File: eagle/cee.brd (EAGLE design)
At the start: 50 x 80 mm, 54 parts, among them IC1 IC1, J1 SOLDERJUMPERNC2

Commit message: Clean up around DAC
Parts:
- moved DAC 3.16 mm to (10.0, 32.0)
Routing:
- net 2.5VREF: track 82.8 -> 71.2 mm, vias 4 -> 3
- net LDAC: track 3.73 -> 6.99 mm
- net VOUT-B: track 22.4 -> 25.7 mm
- net VOUT-A: track 38.5 -> 41.2 mm
- net CS: track 14.9 -> 17.3 mm
- net SCK: track 15.2 -> 17.5 mm
- net MOSI: track 15.6 -> 17.6 mm
- net 5V: track 202.6 -> 203.4 mm, vias 8 -> 9
- net GND: vias 22 -> 23

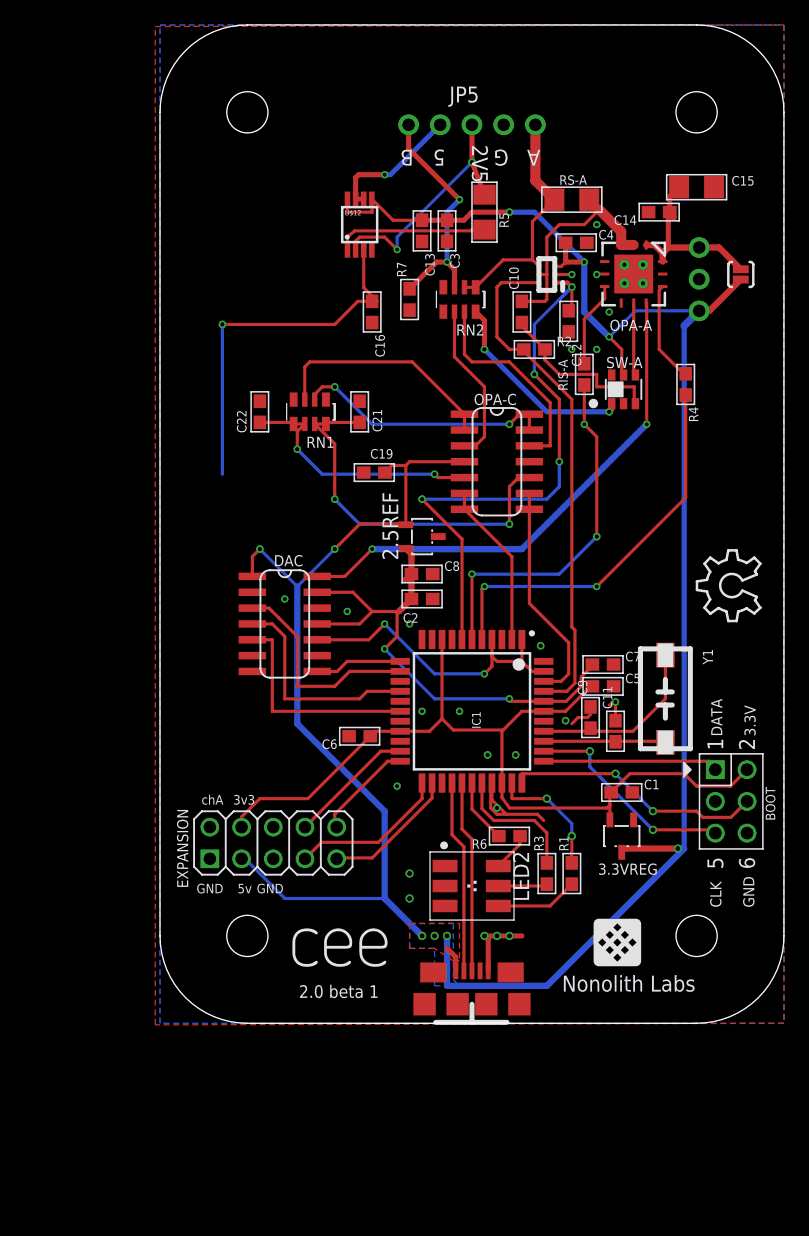
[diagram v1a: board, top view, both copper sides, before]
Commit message: Clean up, route digital lines
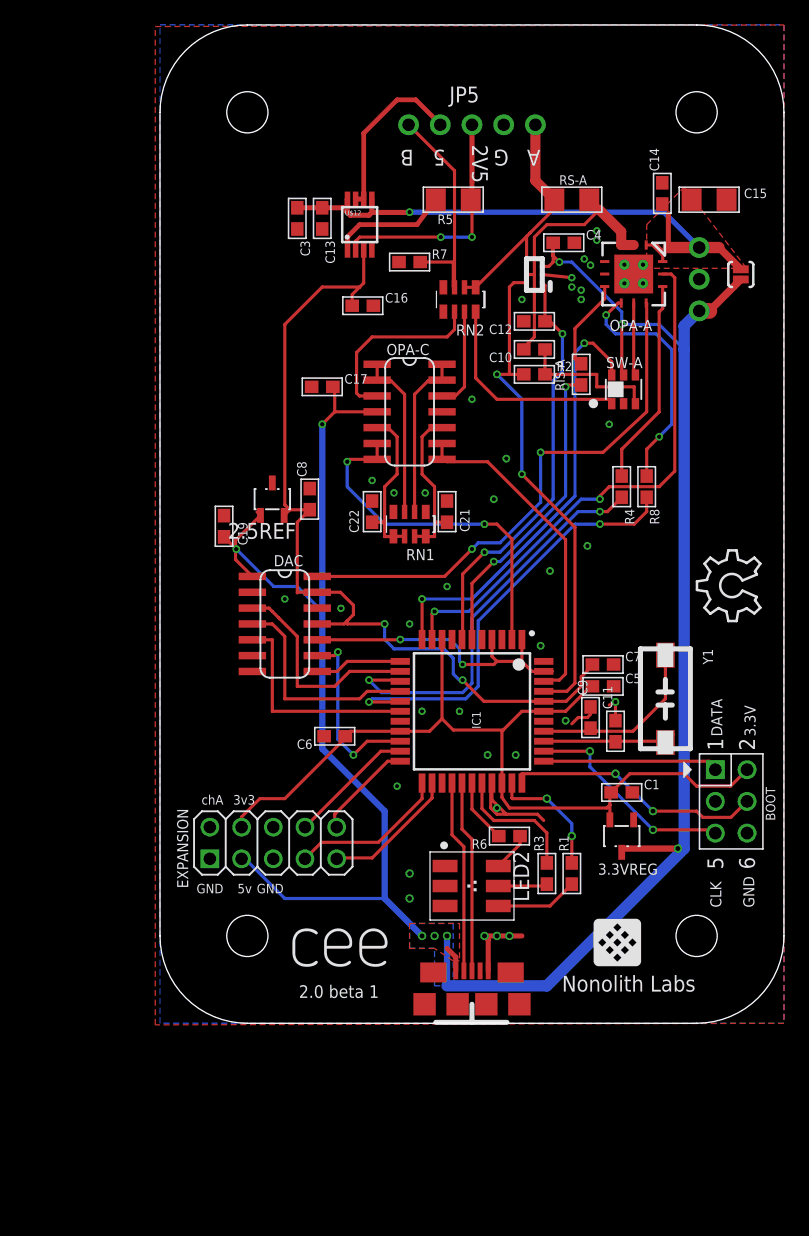
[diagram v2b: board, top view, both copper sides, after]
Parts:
- removed C2: .01uF, nonolith:0603
- added C17: .1uF, nonolith:0603
- added R8: 10ko, nonolith:0603
- moved C19 12.8 mm to (5.13, 39.8), turned to 90 degrees
- moved 2.5REF 12.4 mm to (9.00, 42.0), turned to 180 degrees
- moved C22 12.0 mm to (17.0, 41.0)
- moved RN1 12.0 mm to (20.0, 40.0)
- moved C3 12.0 mm to (11.0, 64.5)
- moved C8 10.8 mm to (12.0, 42.0), turned to 90 degrees
- moved C21 10.6 mm to (23.0, 41.0)
- moved R4 9.67 mm to (37.0, 43.0)
- moved C13 8.06 mm to (13.0, 64.5)
- moved OPA-C 8.06 mm to (20.0, 49.0)
- moved C10 3.16 mm to (30.0, 54.0), turned to 180 degrees
- moved R7 3.00 mm to (20.0, 61.0), turned to 0 degrees
- moved C12 2.75 mm to (30.0, 56.2), turned to 180 degrees
- moved R5 2.69 mm to (23.5, 66.0), turned to 0 degrees
- moved C6 2.00 mm to (14.0, 23.0)
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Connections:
- new net IFLAG-A: OPA-A.7, R8.1
- new net IFLAG-P: IC1.16, R8.2
- net 2.5VREF: no longer C2.1
- net 5V: now also C17.2; no longer C13.1, C3.1, U$12.5, U$12.8
- net 5V-EXT: now also C13.1, C3.1, U$12.5, U$12.8
- net DAC-SHDN: now also IC1.20
- net EN-OPA-A: now also IC1.10
- net GND: now also C17.1; no longer C2.2
- net SWMODE-A: now also IC1.11
- net TFLAG-P: now also IC1.14; no longer IC1.5
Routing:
- net EN-OPA-A: track 0.00 -> 43.0 mm, vias 0 -> 2
- net SWMODE-A: track 0.00 -> 35.3 mm, vias 0 -> 2
- net IFLAG-P: track 0.00 -> 35.3 mm, vias 0 -> 2
- net 5V-EXT: track 15.9 -> 48.0 mm, vias 0 -> 1
- net IFLAG-A: track 0.00 -> 19.4 mm, vias 0 -> 2
- net 5V: track 203.4 -> 186.0 mm, vias 9 -> 8
- net N$1: track 30.1 -> 13.3 mm, vias 2 -> 0
- net ADC-B: track 13.3 -> 28.7 mm, vias 0 -> 2
- net DAC-SHDN: track 0.00 -> 14.7 mm, vias 0 -> 2
- net CSA-VREF: track 47.0 -> 33.6 mm, vias 4 -> 2
- net SMUP-A: track 17.0 -> 8.13 mm
- net ADC-A: track 18.0 -> 26.7 mm
- net TFLAG-A: track 8.09 -> 16.6 mm
- net BUFF-A: track 20.7 -> 13.4 mm, vias 2 -> 0
- net N$2: track 20.3 -> 13.3 mm, vias 2 -> 0
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- added copper zone on layer 1, net 5V-EXT

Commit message: Clean up silkscreen, add GND vias
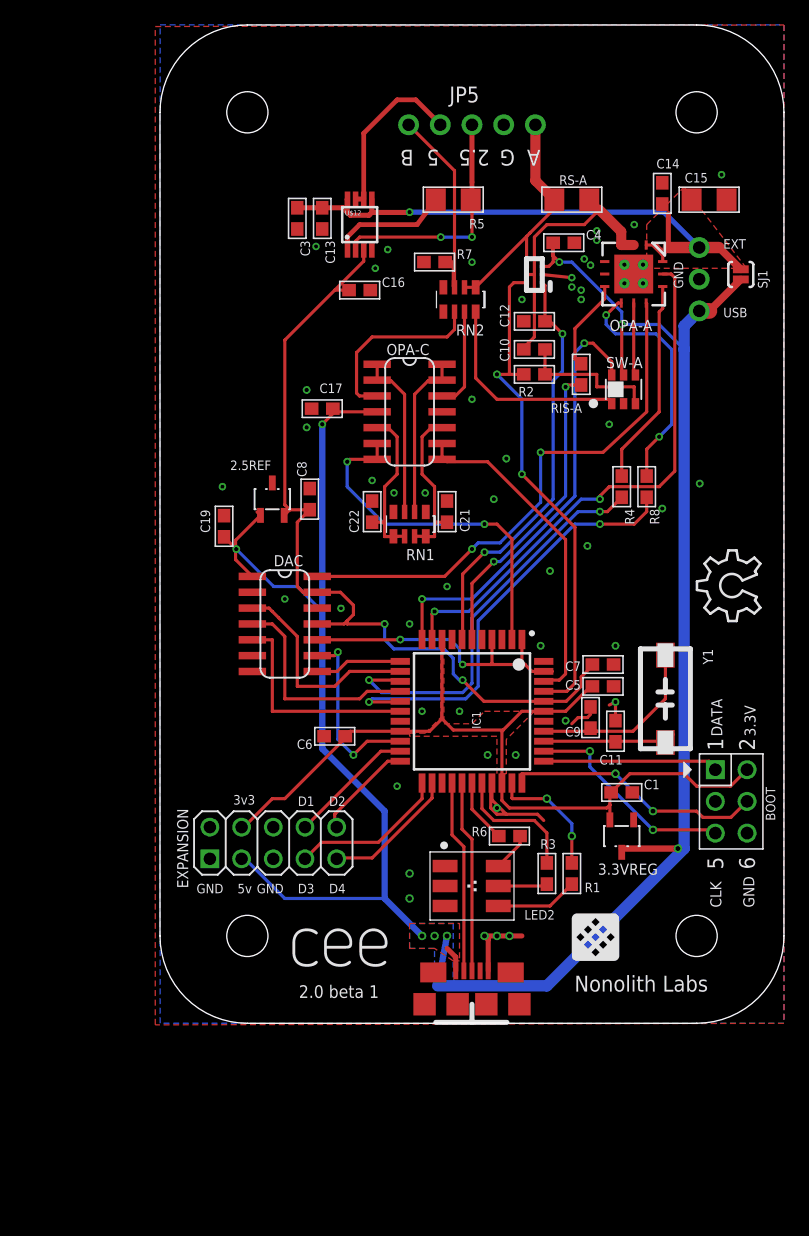
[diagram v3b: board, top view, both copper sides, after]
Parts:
- moved R7 2.00 mm to (22.0, 61.0)
- moved U$3 1.80 mm to (33.0, 5.00)
- moved C17 1.75 mm to (13.0, 49.2)
- moved C16 1.27 mm to (16.0, 58.8)
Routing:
- net 2.5VREF: track 71.1 -> 68.4 mm
- net IN-B: track 19.3 -> 17.3 mm
- net 5V: track 186.0 -> 185.1 mm
- net GND: vias 36 -> 48
- added copper zone on layer 1, net 3.3V
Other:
- board text added: "2.5"
- board text added: "D1"
- board text added: "D2"
- board text added: "D3"
- board text added: "D4"
- board text added: "EXT"
- board text added: "SJ1"
- board text added: "USB"
- board text removed: "2V5"
- board text removed: "chA"

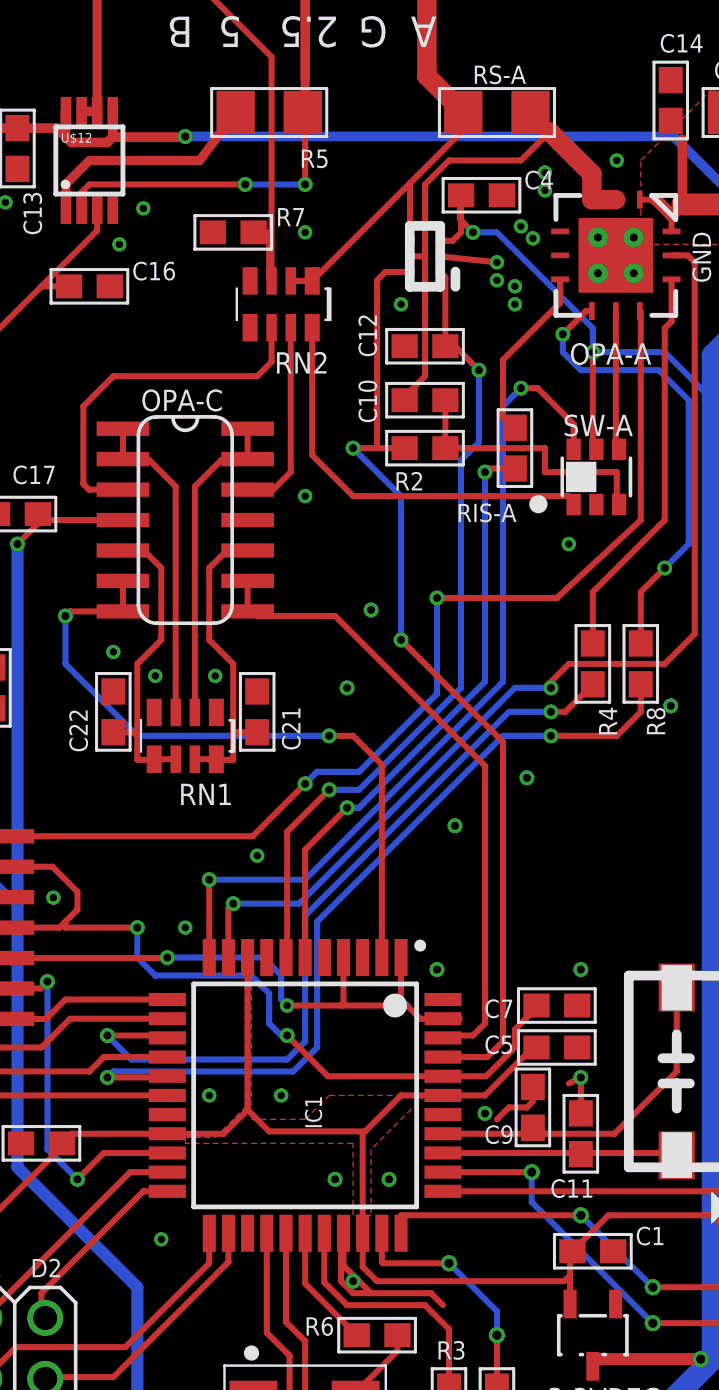
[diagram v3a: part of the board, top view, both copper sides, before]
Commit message: Tweak 3v3 plane to keep GND connection
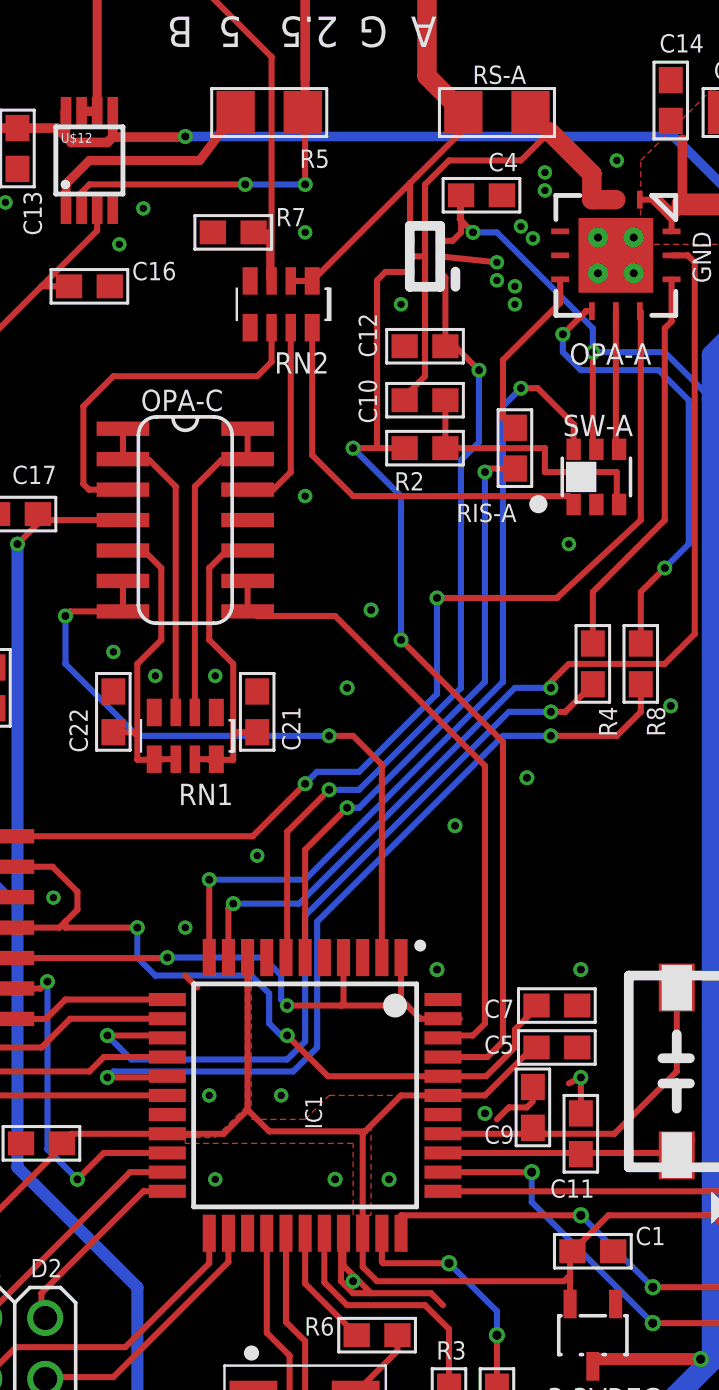
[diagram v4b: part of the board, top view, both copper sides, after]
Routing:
- net GND: track 21.9 -> 22.6 mm
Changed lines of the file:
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@@
 <element name="J1" library="SparkFun" package="SJ_2S-NOTRACE" value="SOLDERJUMPERNC2" x="46.542" y="60.006" smashed="yes" rot="R90"/>
 <element name="C4" library="nonolith" package="0603" value=".1uF" x="32.355" y="62.548" smashed="yes" rot="R180">
-<attribute name="NAME" x="34.133" y="62.802" size="0.762" layer="25" font="vector" ratio="10"/>
+<attribute name="NAME" x="32.633" y="63.552" size="0.762" layer="25" font="vector" ratio="10"/>
 </element>
 <element name="3.3VREG" library="nonolith" package="SOT23-3" value="" x="37" y="15" smashed="yes">
@@
 <via x="24" y="25" extent="1-16" drill="0.305"/>
 <via x="20" y="32" extent="1-16" drill="0.305"/>
-<via x="19" y="19" extent="1-16" drill="0.305"/>
+<via x="21.25" y="21.5" extent="1-16" drill="0.305"/>
 <via x="33.75" y="58" extent="1-16" drill="0.305"/>
 <via x="36" y="48" extent="1-16" drill="0.305"/>
@@
 <via x="12.5" y="62.25" extent="1-16" drill="0.305"/>
 <via x="18.25" y="62" extent="1-16" drill="0.305"/>
+<wire x1="20" y1="30" x2="20.5" y2="29.5" width="0.254" layer="1"/>
 </signal>
 <signal name="PDI-DATA">
@@
 <vertex x="25" y="24"/>
 <vertex x="26" y="25"/>
-<vertex x="30" y="25"/>
-<vertex x="27.75" y="22.75"/>
+<vertex x="29" y="25"/>
+<vertex x="27.75" y="23.75"/>
 <vertex x="27.75" y="20"/>
 <vertex x="27" y="20"/>
